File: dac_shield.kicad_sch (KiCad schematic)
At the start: 27 parts, among them P1 CONN_2, P2 CONN_2, P3 CONN_2, T1 VrefTest, U1 MCP4921, U2 TCA0372, U3 LM741

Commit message: Got PCB mostly updated
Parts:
- R1, R2, R3, R4, R5, R6, R7, R8, R9: footprint custom-footprints:SM0603_VIS -> (none)
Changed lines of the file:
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@@
     (property "Reference" "R4" (id 0) (at 118.11 130.81 90))
     (property "Value" "10k" (id 1) (at 118.11 135.89 90))
-    (property "Footprint" "custom-footprints:SM0603_VIS" (id 2) (at 118.364 132.334 90)
+    (property "Footprint" "" (id 2) (at 118.364 132.334 90)
       (effects (font (size 1.27 1.27)) hide)
     )
@@
     (property "Reference" "R6" (id 0) (at 160.02 129.54 90))
     (property "Value" "33k" (id 1) (at 160.02 134.62 90))
-    (property "Footprint" "custom-footprints:SM0603_VIS" (id 2) (at 160.274 131.064 90)
+    (property "Footprint" "" (id 2) (at 160.274 131.064 90)
       (effects (font (size 1.27 1.27)) hide)
     )
@@
     (property "Reference" "R5" (id 0) (at 132.08 140.97 90))
     (property "Value" "12k" (id 1) (at 137.16 140.97 90))
-    (property "Footprint" "custom-footprints:SM0603_VIS" (id 2) (at 133.604 140.716 90)
+    (property "Footprint" "" (id 2) (at 133.604 140.716 90)
       (effects (font (size 1.27 1.27)) hide)
     )
@@
     (property "Reference" "R3" (id 0) (at 99.06 115.57 90))
     (property "Value" "10k" (id 1) (at 99.06 120.65 90))
-    (property "Footprint" "custom-footprints:SM0603_VIS" (id 2) (at 99.314 117.094 90)
+    (property "Footprint" "" (id 2) (at 99.314 117.094 90)
       (effects (font (size 1.27 1.27)) hide)
     )
@@
     (property "Reference" "R1" (id 0) (at 33.02 109.22 90))
     (property "Value" "22k" (id 1) (at 38.1 109.22 90))
-    (property "Footprint" "custom-footprints:SM0603_VIS" (id 2) (at 34.544 108.966 90)
+    (property "Footprint" "" (id 2) (at 34.544 108.966 90)
       (effects (font (size 1.27 1.27)) hide)
     )
@@
     (property "Reference" "R2" (id 0) (at 33.02 124.46 90))
     (property "Value" "10k" (id 1) (at 38.1 124.46 90))
-    (property "Footprint" "custom-footprints:SM0603_VIS" (id 2) (at 34.544 124.206 90)
+    (property "Footprint" "" (id 2) (at 34.544 124.206 90)
       (effects (font (size 1.27 1.27)) hide)
     )
@@
     (property "Reference" "R7" (id 0) (at 196.85 33.02 90))
     (property "Value" "1k" (id 1) (at 201.93 33.02 90))
-    (property "Footprint" "custom-footprints:SM0603_VIS" (id 2) (at 198.374 32.766 90)
+    (property "Footprint" "" (id 2) (at 198.374 32.766 90)
       (effects (font (size 1.27 1.27)) hide)
     )
@@
     (property "Reference" "R8" (id 0) (at 205.74 33.02 90))
     (property "Value" "1k" (id 1) (at 210.82 33.02 90))
-    (property "Footprint" "custom-footprints:SM0603_VIS" (id 2) (at 207.264 32.766 90)
+    (property "Footprint" "" (id 2) (at 207.264 32.766 90)
       (effects (font (size 1.27 1.27)) hide)
     )
@@
     (property "Reference" "R9" (id 0) (at 219.71 33.02 90))
     (property "Value" "1k" (id 1) (at 224.79 33.02 90))
-    (property "Footprint" "custom-footprints:SM0603_VIS" (id 2) (at 221.234 32.766 90)
+    (property "Footprint" "" (id 2) (at 221.234 32.766 90)
       (effects (font (size 1.27 1.27)) hide)
     )
@@
     )
     (path "/00000000-0000-0000-0000-000051e30b0d"
-      (reference "R1") (unit 1) (value "22k") (footprint "custom-footprints:SM0603_VIS")
+      (reference "R1") (unit 1) (value "22k") (footprint "Resistor_SMD:R_0603_1608Metric")
     )
     (path "/00000000-0000-0000-0000-000051e30b19"
-      (reference "R2") (unit 1) (value "10k") (footprint "custom-footprints:SM0603_VIS")
+      (reference "R2") (unit 1) (value "10k") (footprint "Resistor_SMD:R_0603_1608Metric")
     )
     (path "/00000000-0000-0000-0000-000051e3081f"
-      (reference "R3") (unit 1) (value "10k") (footprint "custom-footprints:SM0603_VIS")
+      (reference "R3") (unit 1) (value "10k") (footprint "Resistor_SMD:R_0603_1608Metric")
     )
     (path "/00000000-0000-0000-0000-000051e30590"
-      (reference "R4") (unit 1) (value "10k") (footprint "custom-footprints:SM0603_VIS")
+      (reference "R4") (unit 1) (value "10k") (footprint "Resistor_SMD:R_0603_1608Metric")
     )
     (path "/00000000-0000-0000-0000-000051e307bd"
-      (reference "R5") (unit 1) (value "12k") (footprint "custom-footprints:SM0603_VIS")
+      (reference "R5") (unit 1) (value "12k") (footprint "Resistor_SMD:R_0603_1608Metric")
     )
     (path "/00000000-0000-0000-0000-000051e30757"
-      (reference "R6") (unit 1) (value "33k") (footprint "custom-footprints:SM0603_VIS")
+      (reference "R6") (unit 1) (value "33k") (footprint "Resistor_SMD:R_0603_1608Metric")
     )
     (path "/00000000-0000-0000-0000-000051e8268f"
-      (reference "R7") (unit 1) (value "1k") (footprint "custom-footprints:SM0603_VIS")
+      (reference "R7") (unit 1) (value "1k") (footprint "Resistor_SMD:R_0603_1608Metric")
     )
     (path "/00000000-0000-0000-0000-000051e827a8"
-      (reference "R8") (unit 1) (value "1k") (footprint "custom-footprints:SM0603_VIS")
+      (reference "R8") (unit 1) (value "1k") (footprint "Resistor_SMD:R_0603_1608Metric")
     )
     (path "/00000000-0000-0000-0000-000051e82914"
-      (reference "R9") (unit 1) (value "1k") (footprint "custom-footprints:SM0603_VIS")
+      (reference "R9") (unit 1) (value "1k") (footprint "Resistor_SMD:R_0603_1608Metric")
     )
     (path "/00000000-0000-0000-0000-000051e30660"

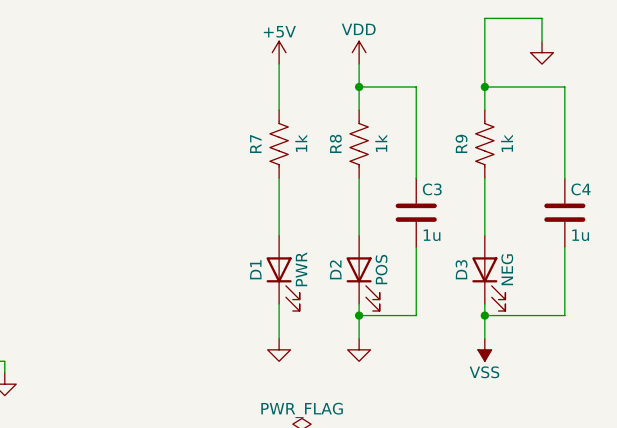
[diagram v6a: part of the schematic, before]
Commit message: Cleaning up tracks, updated led resistors
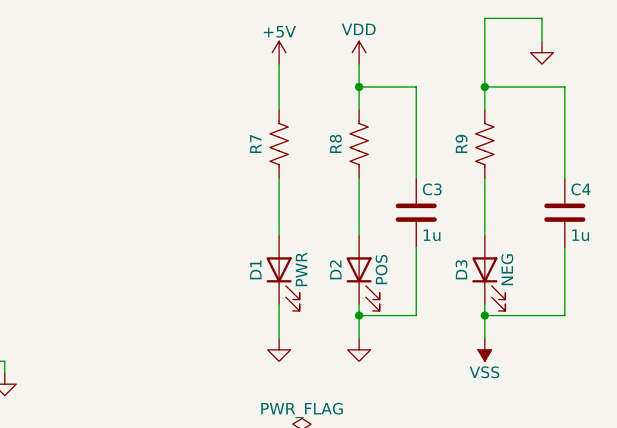
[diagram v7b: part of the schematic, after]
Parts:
- D1, D2, D3: footprint (none) -> LED_SMD:LED_0603_1608Metric
- R1, R2, R3, R4, R5, R6: footprint (none) -> Resistor_SMD:R_0603_1608Metric
- R7, R8, R9: value 1k -> (none); footprint (none) -> Resistor_SMD:R_0603_1608Metric
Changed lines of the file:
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@@
     (property "Reference" "R4" (id 0) (at 118.11 130.81 90))
     (property "Value" "10k" (id 1) (at 118.11 135.89 90))
-    (property "Footprint" "" (id 2) (at 118.364 132.334 90)
+    (property "Footprint" "Resistor_SMD:R_0603_1608Metric" (id 2) (at 118.364 132.334 90)
       (effects (font (size 1.27 1.27)) hide)
     )
@@
     (property "Reference" "R6" (id 0) (at 160.02 129.54 90))
     (property "Value" "33k" (id 1) (at 160.02 134.62 90))
-    (property "Footprint" "" (id 2) (at 160.274 131.064 90)
+    (property "Footprint" "Resistor_SMD:R_0603_1608Metric" (id 2) (at 160.274 131.064 90)
       (effects (font (size 1.27 1.27)) hide)
     )
@@
     (property "Reference" "R5" (id 0) (at 132.08 140.97 90))
     (property "Value" "12k" (id 1) (at 137.16 140.97 90))
-    (property "Footprint" "" (id 2) (at 133.604 140.716 90)
+    (property "Footprint" "Resistor_SMD:R_0603_1608Metric" (id 2) (at 133.604 140.716 90)
       (effects (font (size 1.27 1.27)) hide)
     )
@@
     (property "Reference" "R3" (id 0) (at 99.06 115.57 90))
     (property "Value" "10k" (id 1) (at 99.06 120.65 90))
-    (property "Footprint" "" (id 2) (at 99.314 117.094 90)
+    (property "Footprint" "Resistor_SMD:R_0603_1608Metric" (id 2) (at 99.314 117.094 90)
       (effects (font (size 1.27 1.27)) hide)
     )
@@
     (property "Reference" "R1" (id 0) (at 33.02 109.22 90))
     (property "Value" "22k" (id 1) (at 38.1 109.22 90))
-    (property "Footprint" "" (id 2) (at 34.544 108.966 90)
+    (property "Footprint" "Resistor_SMD:R_0603_1608Metric" (id 2) (at 34.544 108.966 90)
       (effects (font (size 1.27 1.27)) hide)
     )
@@
     (property "Reference" "R2" (id 0) (at 33.02 124.46 90))
     (property "Value" "10k" (id 1) (at 38.1 124.46 90))
-    (property "Footprint" "" (id 2) (at 34.544 124.206 90)
+    (property "Footprint" "Resistor_SMD:R_0603_1608Metric" (id 2) (at 34.544 124.206 90)
       (effects (font (size 1.27 1.27)) hide)
     )
@@
     (property "Reference" "D1" (id 0) (at 196.85 46.99 0))
     (property "Value" "PWR" (id 1) (at 201.93 46.99 0))
-    (property "Footprint" "" (id 2) (at 199.39 46.99 0)
+    (property "Footprint" "LED_SMD:LED_0603_1608Metric" (id 2) (at 199.39 46.99 0)
       (effects (font (size 1.27 1.27)) hide)
     )
@@
     (in_bom yes) (on_board yes)
     (property "Reference" "R7" (id 0) (at 196.85 33.02 90))
-    (property "Value" "1k" (id 1) (at 201.93 33.02 90))
-    (property "Footprint" "" (id 2) (at 198.374 32.766 90)
+    (property "Value" "" (id 1) (at 201.93 33.02 90))
+    (property "Footprint" "Resistor_SMD:R_0603_1608Metric" (id 2) (at 198.374 32.766 90)
       (effects (font (size 1.27 1.27)) hide)
     )
@@
     (in_bom yes) (on_board yes)
     (property "Reference" "R8" (id 0) (at 205.74 33.02 90))
-    (property "Value" "1k" (id 1) (at 210.82 33.02 90))
-    (property "Footprint" "" (id 2) (at 207.264 32.766 90)
+    (property "Value" "" (id 1) (at 210.82 33.02 90))
+    (property "Footprint" "Resistor_SMD:R_0603_1608Metric" (id 2) (at 207.264 32.766 90)
       (effects (font (size 1.27 1.27)) hide)
     )
@@
     (property "Reference" "D2" (id 0) (at 205.74 46.99 0))
     (property "Value" "POS" (id 1) (at 210.82 46.99 0))
-    (property "Footprint" "" (id 2) (at 208.28 46.99 0)
+    (property "Footprint" "LED_SMD:LED_0603_1608Metric" (id 2) (at 208.28 46.99 0)
       (effects (font (size 1.27 1.27)) hide)
     )
@@
     (in_bom yes) (on_board yes)
     (property "Reference" "R9" (id 0) (at 219.71 33.02 90))
-    (property "Value" "1k" (id 1) (at 224.79 33.02 90))
-    (property "Footprint" "" (id 2) (at 221.234 32.766 90)
+    (property "Value" "" (id 1) (at 224.79 33.02 90))
+    (property "Footprint" "Resistor_SMD:R_0603_1608Metric" (id 2) (at 221.234 32.766 90)
       (effects (font (size 1.27 1.27)) hide)
     )
@@
     (property "Reference" "D3" (id 0) (at 219.71 46.99 0))
     (property "Value" "NEG" (id 1) (at 224.79 46.99 0))
-    (property "Footprint" "" (id 2) (at 222.25 46.99 0)
+    (property "Footprint" "LED_SMD:LED_0603_1608Metric" (id 2) (at 222.25 46.99 0)
       (effects (font (size 1.27 1.27)) hide)
     )
@@
     )
     (path "/00000000-0000-0000-0000-000051e8268f"
-      (reference "R7") (unit 1) (value "1k") (footprint "Resistor_SMD:R_0603_1608Metric")
+      (reference "R7") (unit 1) (value "2.2k") (footprint "Resistor_SMD:R_0603_1608Metric")
     )
     (path "/00000000-0000-0000-0000-000051e827a8"
-      (reference "R8") (unit 1) (value "1k") (footprint "Resistor_SMD:R_0603_1608Metric")
+      (reference "R8") (unit 1) (value "2.2k") (footprint "Resistor_SMD:R_0603_1608Metric")
     )
     (path "/00000000-0000-0000-0000-000051e82914"
-      (reference "R9") (unit 1) (value "1k") (footprint "Resistor_SMD:R_0603_1608Metric")
+      (reference "R9") (unit 1) (value "2.2") (footprint "Resistor_SMD:R_0603_1608Metric")
     )
     (path "/00000000-0000-0000-0000-000051e30660"
